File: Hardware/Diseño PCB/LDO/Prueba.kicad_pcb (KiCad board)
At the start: 2 copper layers, 53 parts, among them J1 Vo, Q1 2N3904, Q10 BC557, Q11 BC547, Q12 BC557, Q13 2N3906, Q14 2N3904, Q15 2N3906, Q16 2N3904, Q17 2N3906, Q18 2N3904, Q19 2N3904, Q2 2N3904, Q3 2N3904, Q4 2N3906, Q5 2N3906, Q6 2N3904, Q7 2N3904, Q8 IRF4905, Q9 BC547, U1 TL431LP, U4 LM324

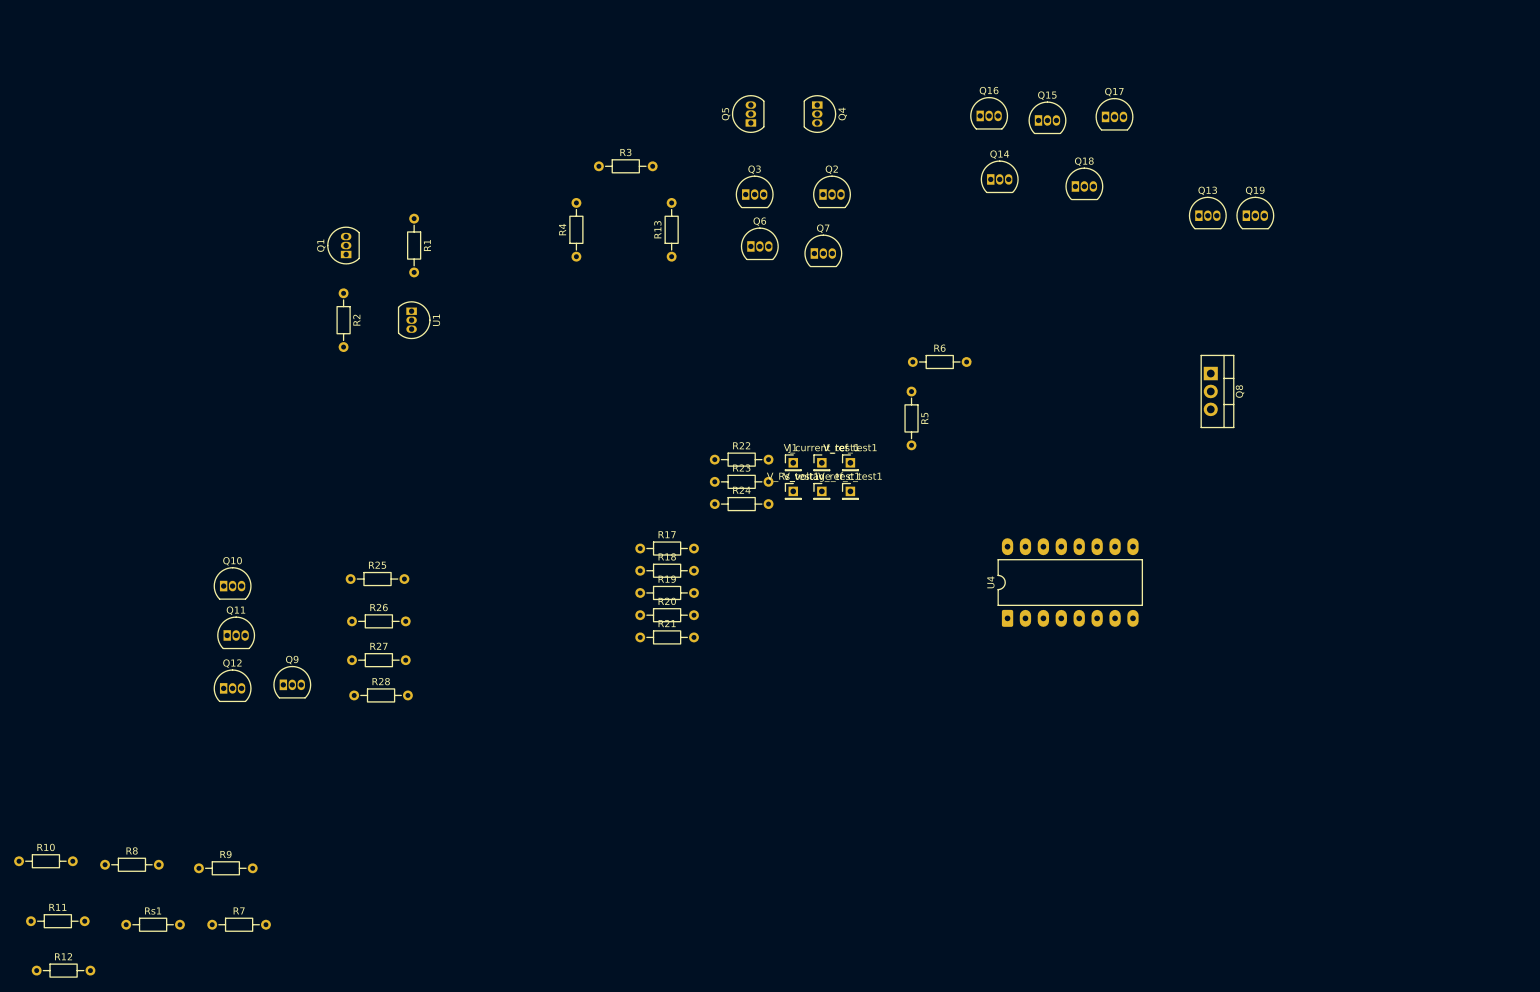
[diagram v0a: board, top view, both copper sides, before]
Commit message: Agrupación de modulos en diseño de PCB
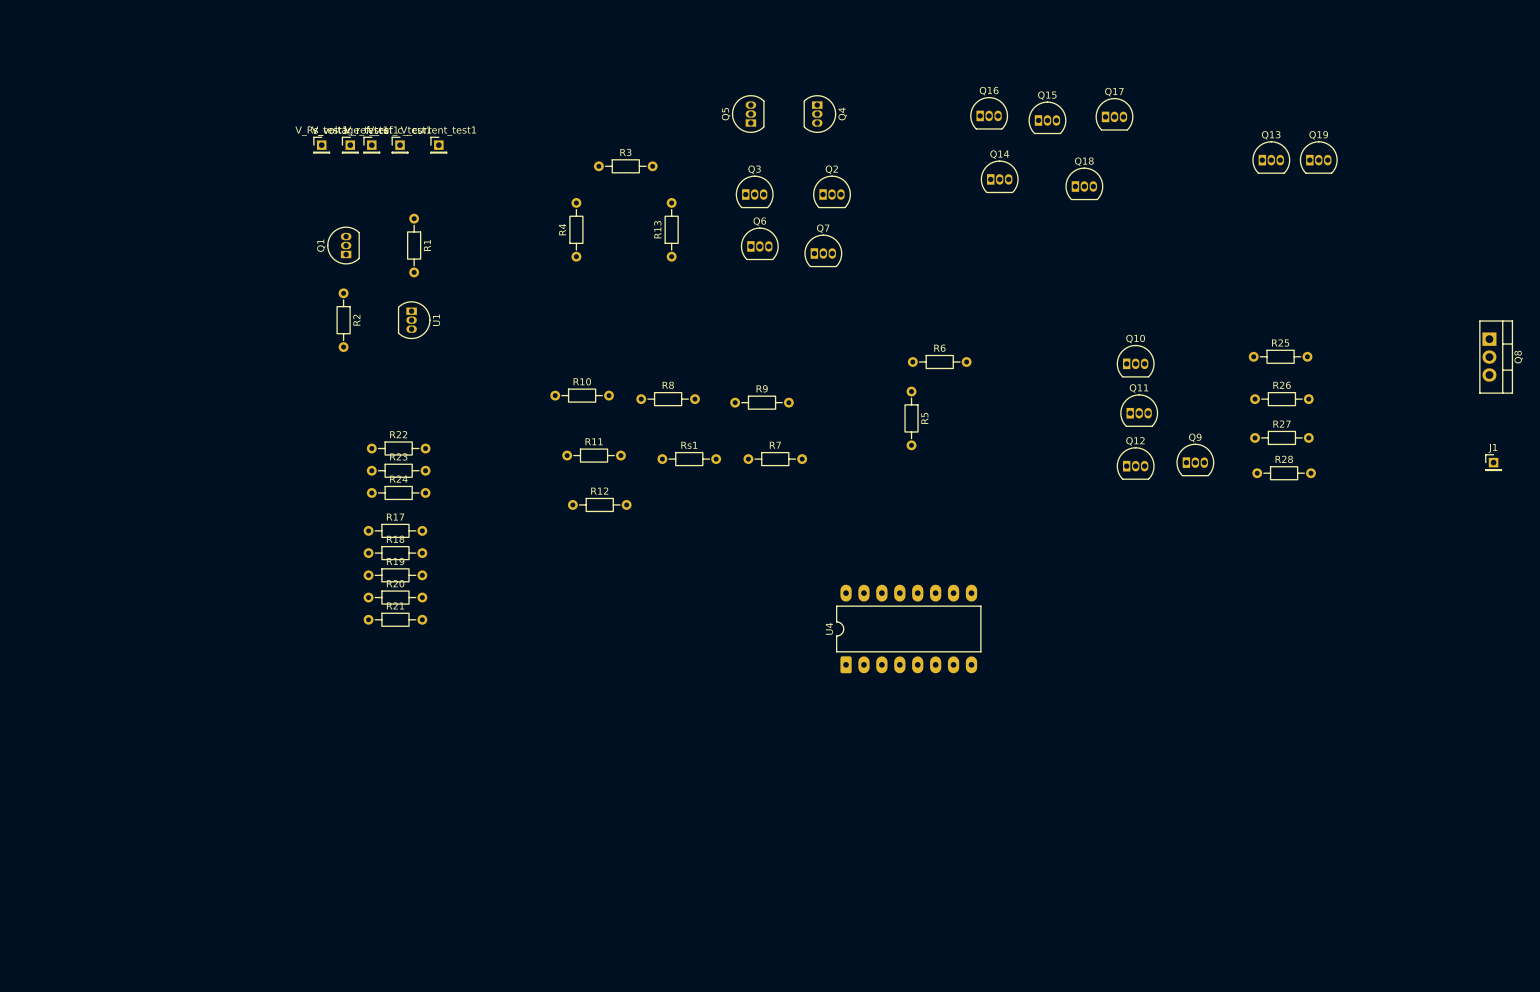
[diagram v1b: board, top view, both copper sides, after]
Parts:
- moved Q10 131.8 mm to (195.0, 65.0)
- moved Q11 131.8 mm to (195.5, 72.0)
- moved Q12 131.8 mm to (195.0, 79.5)
- moved Q9 131.8 mm to (203.5, 79.0)
- moved R25 131.8 mm to (213.0, 64.0)
- moved R26 131.8 mm to (213.2, 70.0)
- moved R27 131.8 mm to (213.2, 75.5)
- moved R28 131.8 mm to (213.5, 80.5)
- moved R10 100.7 mm to (114.0, 69.5)
- moved R11 100.7 mm to (115.7, 78.0)
- moved R12 100.7 mm to (116.5, 85.0)
- moved R7 100.7 mm to (141.4, 78.5)
- moved R8 100.7 mm to (126.2, 70.0)
- moved R9 100.7 mm to (139.5, 70.5)
- moved Rs1 100.7 mm to (129.2, 78.5)
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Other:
- board text added: "Amplificadores Operacionales"
- board text added: "Salida"
- board text added: "Tension de Vref_C"
- board text added: "Tensiónes de referencian"

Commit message: Diseño PCB :  Test con gnd en comun
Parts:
- added GND1: Pin_GND, Connector_PinHeader_2.00mm:PinHeader_1x01_P2.00mm_Vertical, F.Cu at (71.7, 33.0)
- Vo1: renamed from J1; footprint Connector_PinHeader_2.00mm:PinHeader_1x01_P2.00mm_Vertical -> Connector_PinHeader_2.00mm:PinHeader_1x02_P2.00mm_Vertical
- moved V_current_test1 4.80 mm to (102.2, 33.0)
- moved V_ref_c_test1 4.22 mm to (96.1, 33.0)
- moved R17 3.55 mm to (84.2, 87.4)
- moved R18 3.44 mm to (84.2, 90.9)
- moved R24 3.37 mm to (84.7, 83.9)
- moved R19 3.37 mm to (84.2, 94.3)
- moved R20 3.33 mm to (84.2, 97.8)
- moved R23 3.33 mm to (84.7, 80.5)
- moved R21 3.31 mm to (84.2, 101.3)
- moved R22 3.31 mm to (84.7, 77.0)
- moved V_Rs_test1 3.25 mm to (77.8, 33.0)
- moved Q14 3.00 mm to (178.7, 38.9)
- moved Q5 2.77 mm to (143.7, 32.8)
- moved Q4 2.77 mm to (153.1, 30.2)
- moved R12 2.69 mm to (114.0, 84.0)
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
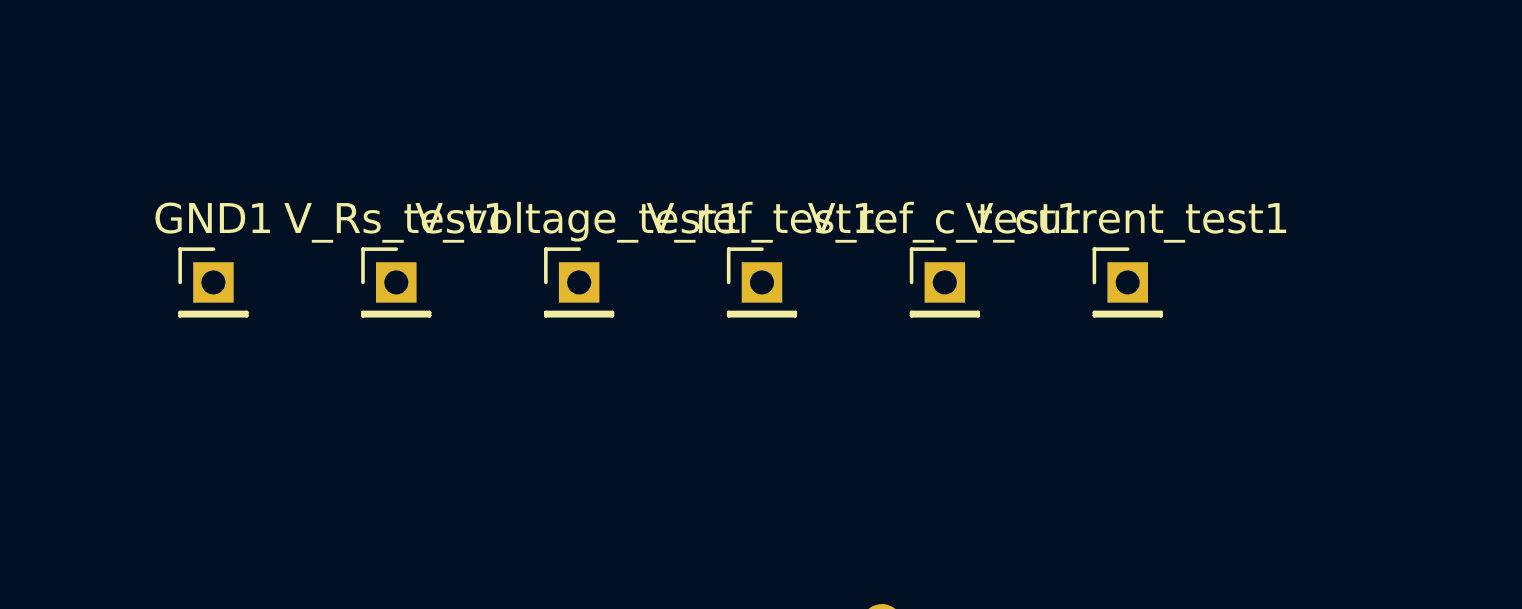
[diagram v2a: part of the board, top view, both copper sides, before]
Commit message: Diseño PCB: Indicador de operacionales dentro de encapsulado
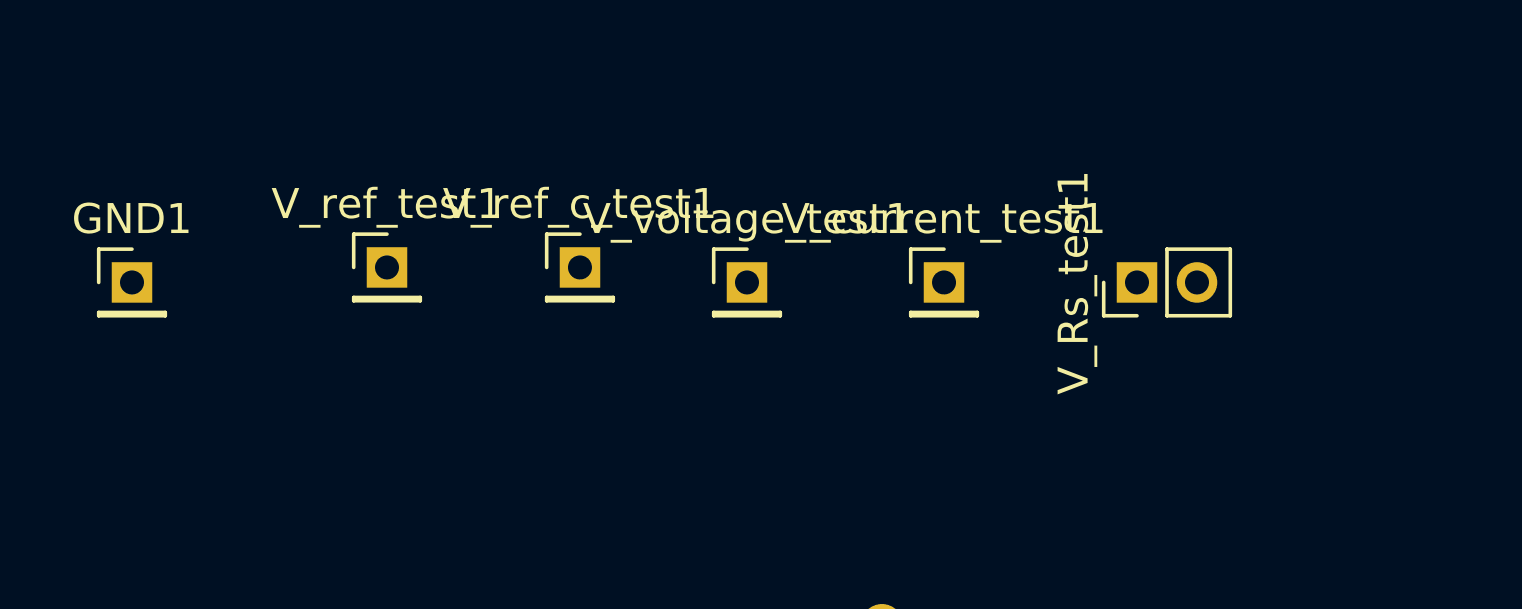
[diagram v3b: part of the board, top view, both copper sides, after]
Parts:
- V_Rs_test1: footprint Connector_PinHeader_2.00mm:PinHeader_1x01_P2.00mm_Vertical -> Connector_PinHeader_2.00mm:PinHeader_1x02_P2.00mm_Vertical
- moved V_Rs_test1 24.7 mm to (102.5, 33.0), turned to 90 degrees
- moved V_ref_test1 12.5 mm to (77.5, 32.5)
- moved V_ref_c_test1 12.2 mm to (83.9, 32.5)
- moved V_current_test1 6.12 mm to (96.1, 33.0)
- moved V_voltage_test1 5.59 mm to (89.5, 33.0)
- moved GND1 2.72 mm to (69.0, 33.0)
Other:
- board text added: "GND"
- board text added: "Tensiónes de Test"
- board text added: "V_ref_C"
- board text added: "V_ref_t"
- board text added: "Vcurrent"
- board text added: "Vrs"
- board text added: "Vvoltage"
- board text removed: "Tensiónes de referencian"
